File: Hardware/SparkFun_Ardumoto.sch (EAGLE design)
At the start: 64 parts, among them U1 ARDUINO, U2 L298, U5 74HC1G04, U6 74HC1G04

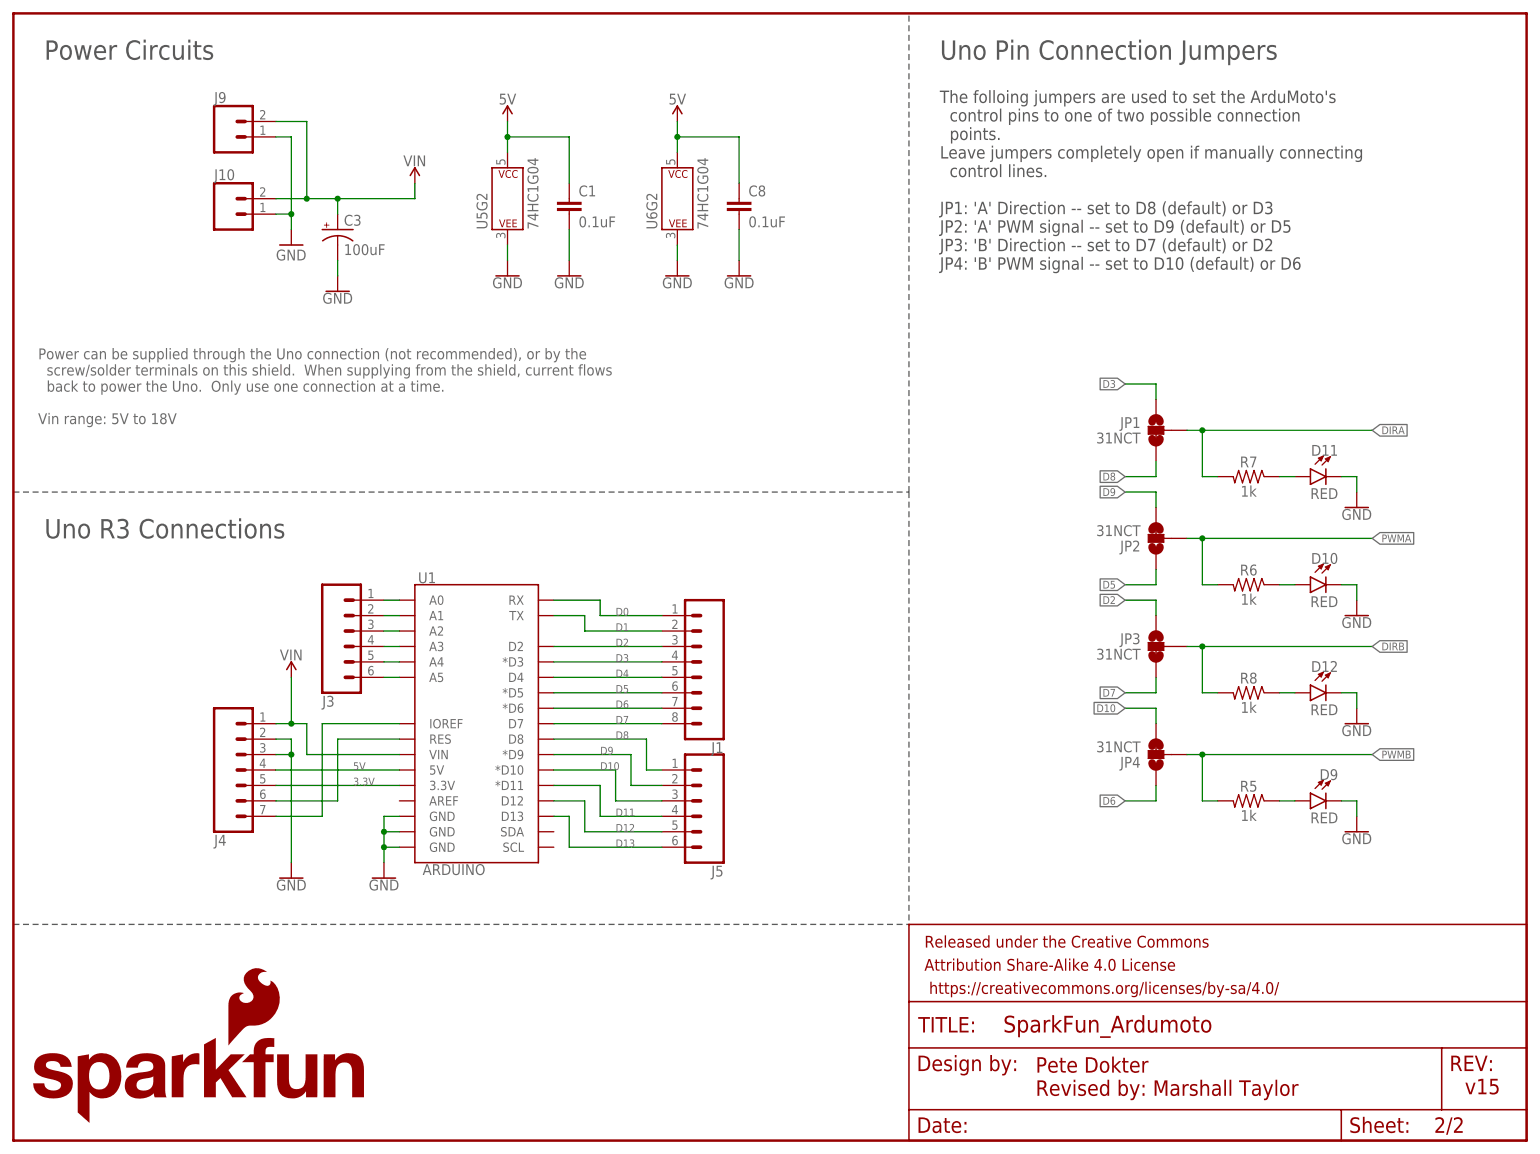
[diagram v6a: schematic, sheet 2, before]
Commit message: Made changes to prototype in preparation for reds
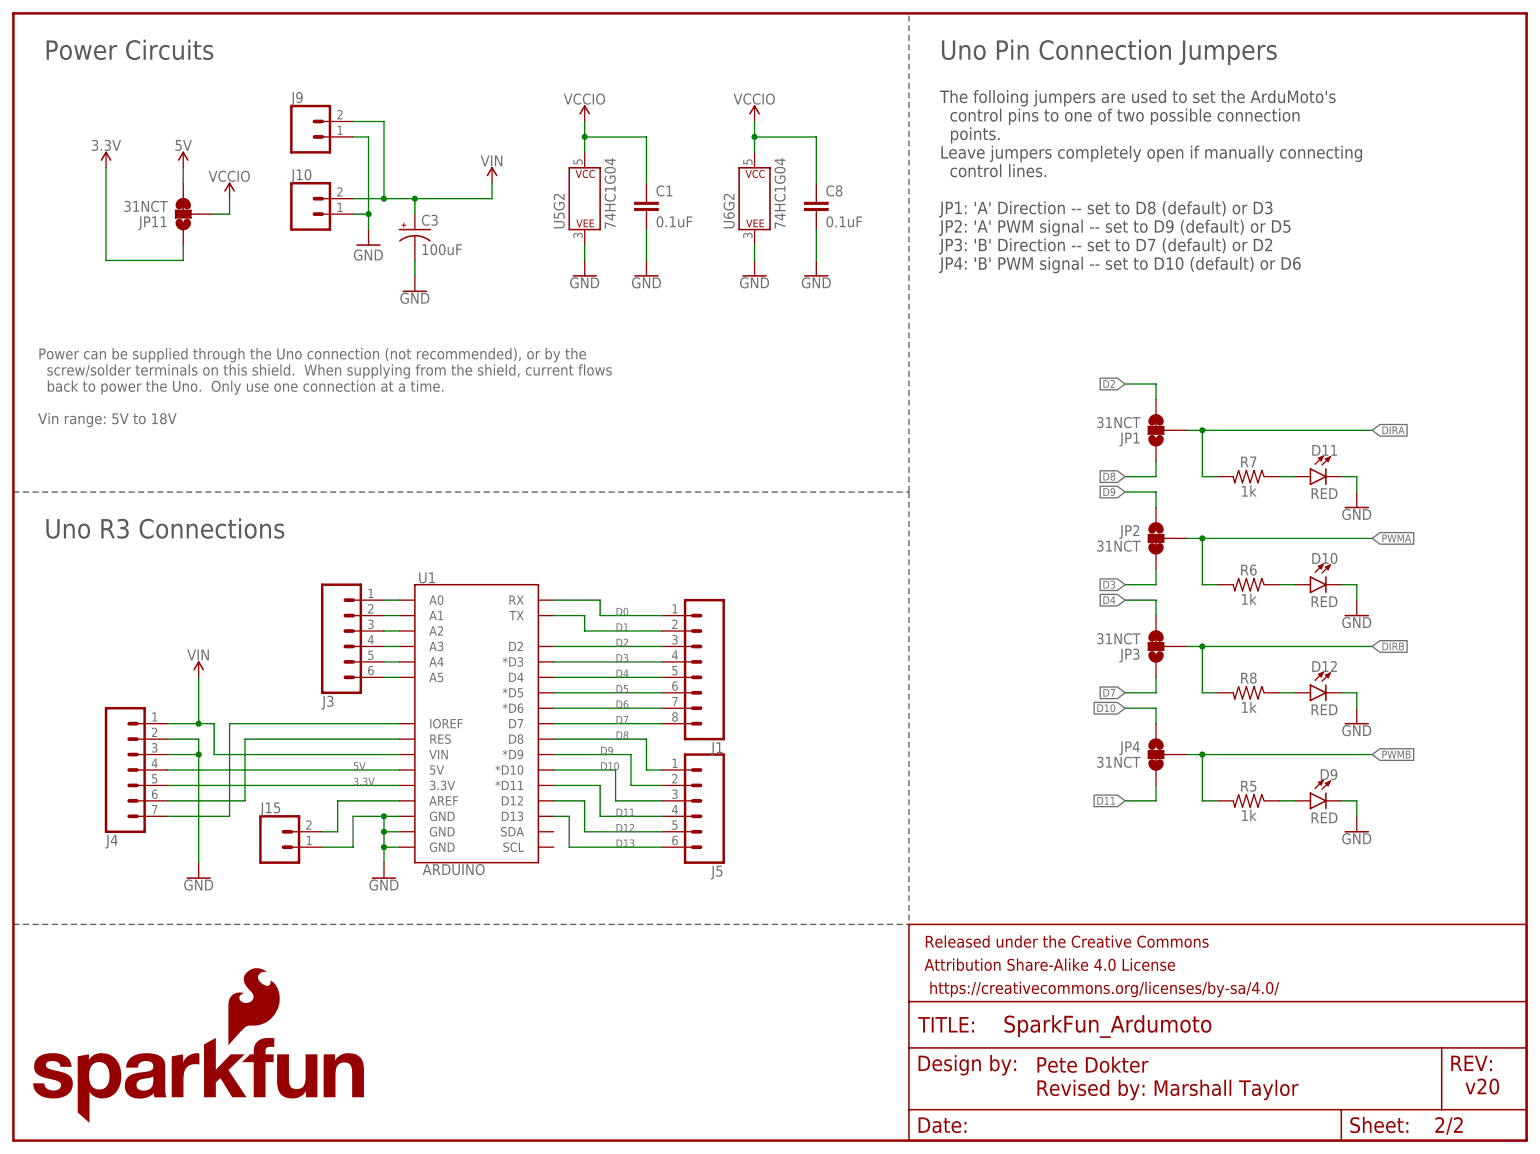
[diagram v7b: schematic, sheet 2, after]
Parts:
- added J15: (no value), SparkFun-Connectors:CONN_021X02_NO_SILK
- added JP11: 31NCT, SparkFun-Jumpers:JUMPER-SMT_3_1-NC_TRACE_SILK
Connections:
- new net N$10: J15.2, U1.AREF
- new net VCCIO: C1.1, C8.1, JP11.2, U2.VSS, U5G2.P$V+, U6G2.P$V+
- net 3.3V: now also JP11.1
- net 5V: now also JP11.3; no longer C1.1, C8.1, U2.VSS, U5G2.P$V+, U6G2.P$V+
- net D10: now also JP4.1; no longer JP4.3
- net D11: now also JP4.3
- net D2: now also JP1.3; no longer JP3.1
- net D3: now also JP2.3; no longer JP1.1
- net D4: now also JP3.3
- net D5: no longer JP2.1
- net D6: no longer JP4.1
- net D7: now also JP3.1; no longer JP3.3
- net D8: now also JP1.1; no longer JP1.3
- net D9: now also JP2.1; no longer JP2.3
- net GND: now also J15.1
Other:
- note added: "v20"
- note removed: "v15"
- moved on the sheet: C1, C3, C8, J10, J4, J9, JP1, JP2, JP3, JP4, U5G2, U6G2

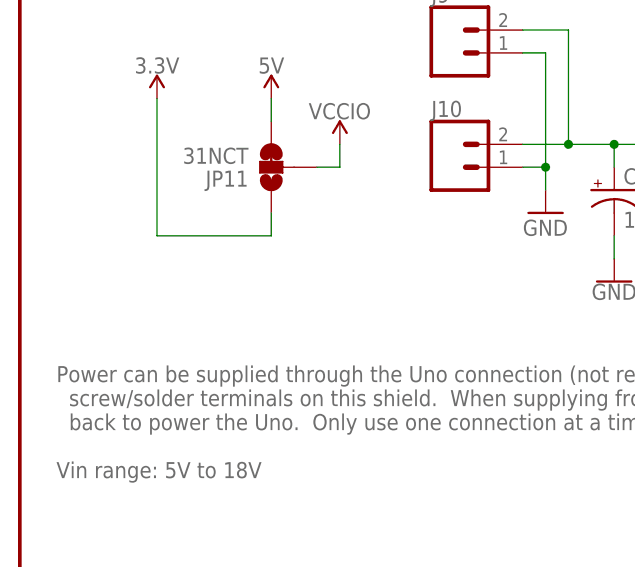
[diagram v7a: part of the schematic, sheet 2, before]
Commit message: Added note on VCCIO and nudged traces
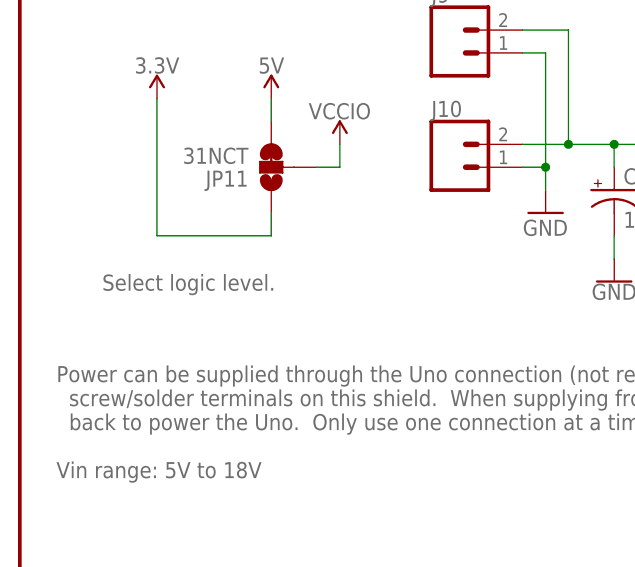
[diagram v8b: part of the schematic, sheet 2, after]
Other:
- note added: "Select logic level."
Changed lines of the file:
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@@
 <text x="5.08" y="99.06" size="3.175" layer="97" font="vector">Uno R3 Connections</text>
 <wire x1="0" y1="35.56" x2="147.32" y2="35.56" width="0.2032" layer="97" style="longdash"/>
+<text x="9.144" y="140.462" size="1.778" layer="95" font="vector" align="top-left">Select logic level.</text>
 </plain>
 <instances>
